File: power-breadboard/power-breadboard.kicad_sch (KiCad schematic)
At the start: 0 parts

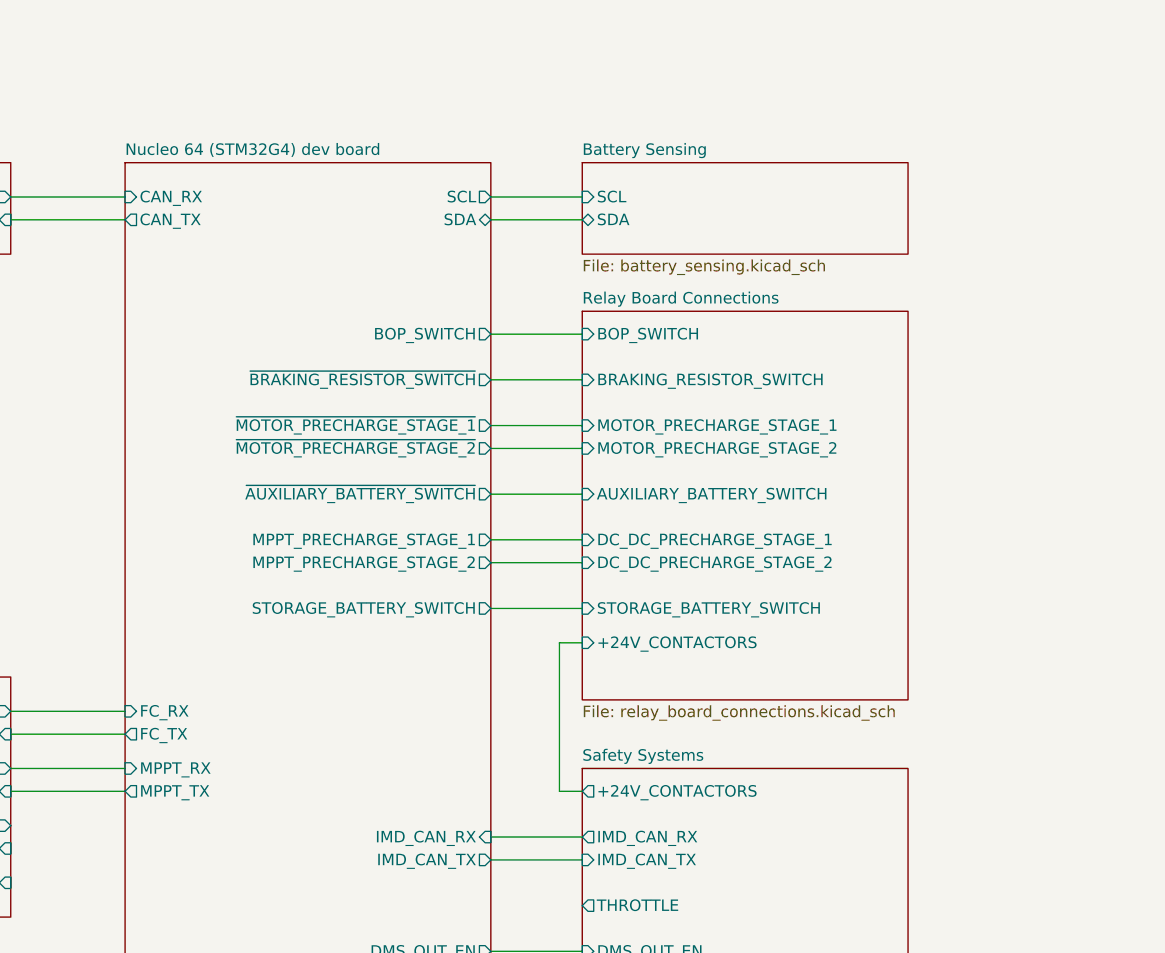
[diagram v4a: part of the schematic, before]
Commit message: power-breadboard: finish relay board connections
Updateed to use separarate relay boards. Also updated hierarchical
labels and sheet pins.
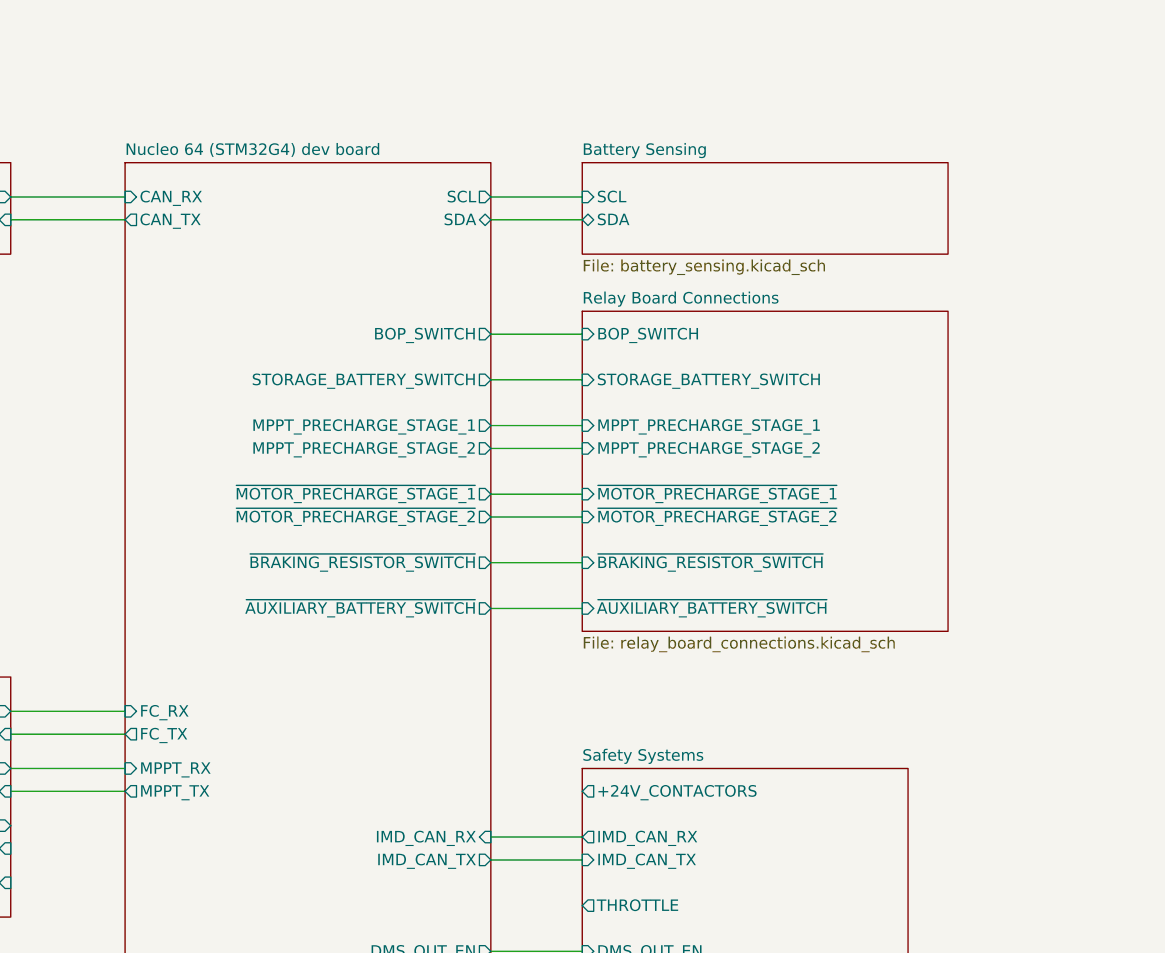
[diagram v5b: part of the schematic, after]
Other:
- sheet Relay Board Connections ports: added MPPT_PRECHARGE_STAGE_1, MPPT_PRECHARGE_STAGE_2, ~{AUXILIARY_BATTERY_SWITCH}, ~{BRAKING_RESISTOR_SWITCH}, ~{MOTOR_PRECHARGE_STAGE_1}, ~{MOTOR_PRECHARGE_STAGE_2}; removed +24V_CONTACTORS, AUXILIARY_BATTERY_SWITCH, BRAKING_RESISTOR_SWITCH, DC_DC_PRECHARGE_STAGE_1, DC_DC_PRECHARGE_STAGE_2, MOTOR_PRECHARGE_STAGE_1, MOTOR_PRECHARGE_STAGE_2
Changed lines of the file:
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@@
 	(wire
 		(pts
-			(xy 147.32 54.61) (xy 157.48 54.61)
+			(xy 147.32 74.93) (xy 157.48 74.93)
 		)
 		(stroke
@@
 	(wire
 		(pts
-			(xy 147.32 80.01) (xy 157.48 80.01)
+			(xy 147.32 54.61) (xy 157.48 54.61)
 		)
 		(stroke
@@
 	(wire
 		(pts
-			(xy 147.32 62.23) (xy 157.48 62.23)
-		)
-		(stroke
-			(width 0)
-			(type default)
-		)
-	)
-	(wire
-		(pts
-			(xy 154.94 100.33) (xy 154.94 83.82)
+			(xy 147.32 69.85) (xy 157.48 69.85)
 		)
 		(stroke
@@
 	(wire
 		(pts
-			(xy 147.32 59.69) (xy 157.48 59.69)
+			(xy 147.32 67.31) (xy 157.48 67.31)
 		)
 		(stroke
@@
 	(wire
 		(pts
-			(xy 147.32 67.31) (xy 157.48 67.31)
+			(xy 147.32 80.01) (xy 157.48 80.01)
 		)
 		(stroke
@@
 	(wire
 		(pts
-			(xy 147.32 74.93) (xy 157.48 74.93)
-		)
-		(stroke
-			(width 0)
-			(type default)
-		)
-	)
-	(wire
-		(pts
-			(xy 157.48 100.33) (xy 154.94 100.33)
+			(xy 147.32 62.23) (xy 157.48 62.23)
 		)
 		(stroke
@@
 	(wire
 		(pts
-			(xy 154.94 83.82) (xy 157.48 83.82)
-		)
-		(stroke
-			(width 0)
-			(type default)
-		)
-	)
-	(wire
-		(pts
-			(xy 147.32 72.39) (xy 157.48 72.39)
+			(xy 147.32 59.69) (xy 157.48 59.69)
 		)
 		(stroke
@@
 	(sheet
 		(at 157.48 30.48)
-		(size 36.195 10.16)
+		(size 40.64 10.16)
 		(exclude_from_sim no)
 		(in_bom yes)
@@
 		)
 		(pin "MPPT_PRECHARGE_STAGE_1" output
-			(at 147.32 72.39 0)
+			(at 147.32 59.69 0)
 			(effects
 				(font
@@
 		)
 		(pin "MPPT_PRECHARGE_STAGE_2" output
-			(at 147.32 74.93 0)
+			(at 147.32 62.23 0)
 			(effects
 				(font
@@
 		)
 		(pin "STORAGE_BATTERY_SWITCH" output
-			(at 147.32 80.01 0)
+			(at 147.32 54.61 0)
 			(effects
 				(font
@@
 		)
 		(pin "~{AUXILIARY_BATTERY_SWITCH}" output
+			(at 147.32 80.01 0)
+			(effects
+				(font
+					(size 1.27 1.27)
+				)
+				(justify right)
+			)
+		)
+		(pin "~{BRAKING_RESISTOR_SWITCH}" output
+			(at 147.32 74.93 0)
+			(effects
+				(font
+					(size 1.27 1.27)
+				)
+				(justify right)
+			)
+		)
+		(pin "~{MOTOR_PRECHARGE_STAGE_1}" output
 			(at 147.32 67.31 0)
 			(effects
@@
 			)
 		)
-		(pin "~{BRAKING_RESISTOR_SWITCH}" output
-			(at 147.32 54.61 0)
-			(effects
-				(font
-					(size 1.27 1.27)
-				)
-				(justify right)
-			)
-		)
-		(pin "~{MOTOR_PRECHARGE_STAGE_1}" output
-			(at 147.32 59.69 0)
-			(effects
-				(font
-					(size 1.27 1.27)
-				)
-				(justify right)
-			)
-		)
 		(pin "~{MOTOR_PRECHARGE_STAGE_2}" output
-			(at 147.32 62.23 0)
+			(at 147.32 69.85 0)
 			(effects
 				(font
@@
 	(sheet
 		(at 157.48 46.99)
-		(size 36.195 43.18)
+		(size 40.64 35.56)
 		(exclude_from_sim no)
 		(in_bom yes)
@@
 		)
 		(property "Sheetfile" "relay_board_connections.kicad_sch"
-			(at 157.48 90.7546 0)
+			(at 157.48 83.1346 0)
 			(show_name no)
 			(do_not_autoplace no)
@@
 		)
 		(pin "STORAGE_BATTERY_SWITCH" input
-			(at 157.48 80.01 180)
-			(effects
-				(font
-					(size 1.27 1.27)
-				)
-				(justify left)
-			)
-		)
-		(pin "DC_DC_PRECHARGE_STAGE_2" input
-			(at 157.48 74.93 180)
-			(effects
-				(font
-					(size 1.27 1.27)
-				)
-				(justify left)
-			)
-		)
-		(pin "DC_DC_PRECHARGE_STAGE_1" input
-			(at 157.48 72.39 180)
-			(effects
-				(font
-					(size 1.27 1.27)
-				)
-				(justify left)
-			)
-		)
-		(pin "AUXILIARY_BATTERY_SWITCH" input
-			(at 157.48 67.31 180)
-			(effects
-				(font
-					(size 1.27 1.27)
-				)
-				(justify left)
-			)
-		)
-		(pin "MOTOR_PRECHARGE_STAGE_2" input
-			(at 157.48 62.23 180)
-			(effects
-				(font
-					(size 1.27 1.27)
-				)
-				(justify left)
-			)
-		)
-		(pin "MOTOR_PRECHARGE_STAGE_1" input
-			(at 157.48 59.69 180)
-			(effects
-				(font
-					(size 1.27 1.27)
-				)
-				(justify left)
-			)
-		)
-		(pin "BRAKING_RESISTOR_SWITCH" input
 			(at 157.48 54.61 180)
 			(effects
@@
 			)
 		)
-		(pin "+24V_CONTACTORS" input
-			(at 157.48 83.82 180)
-			(effects
-				(font
+		(pin "MPPT_PRECHARGE_STAGE_1" input
+			(at 157.48 59.69 180)
+			(effects
+				(font
+					(size 1.27 1.27)
+				)
+				(justify left)
+			)
+		)
+		(pin "MPPT_PRECHARGE_STAGE_2" input
+			(at 157.48 62.23 180)
+			(effects
+				(font
+					(size 1.27 1.27)
+				)
+				(justify left)
+			)
+		)
+		(pin "~{AUXILIARY_BATTERY_SWITCH}" input
+			(at 157.48 80.01 180)
+			(effects
+				(font
+					(size 1.27 1.27)
+				)
+				(justify left)
+			)
+		)
+		(pin "~{BRAKING_RESISTOR_SWITCH}" input
+			(at 157.48 74.93 180)
+			(effects
+				(font
+					(size 1.27 1.27)
+				)
+				(justify left)
+			)
+		)
+		(pin "~{MOTOR_PRECHARGE_STAGE_1}" input
+			(at 157.48 67.31 180)
+			(effects
+				(font
+					(size 1.27 1.27)
+				)
+				(justify left)
+			)
+		)
+		(pin "~{MOTOR_PRECHARGE_STAGE_2}" input
+			(at 157.48 69.85 180)
+			(effects
+				(font

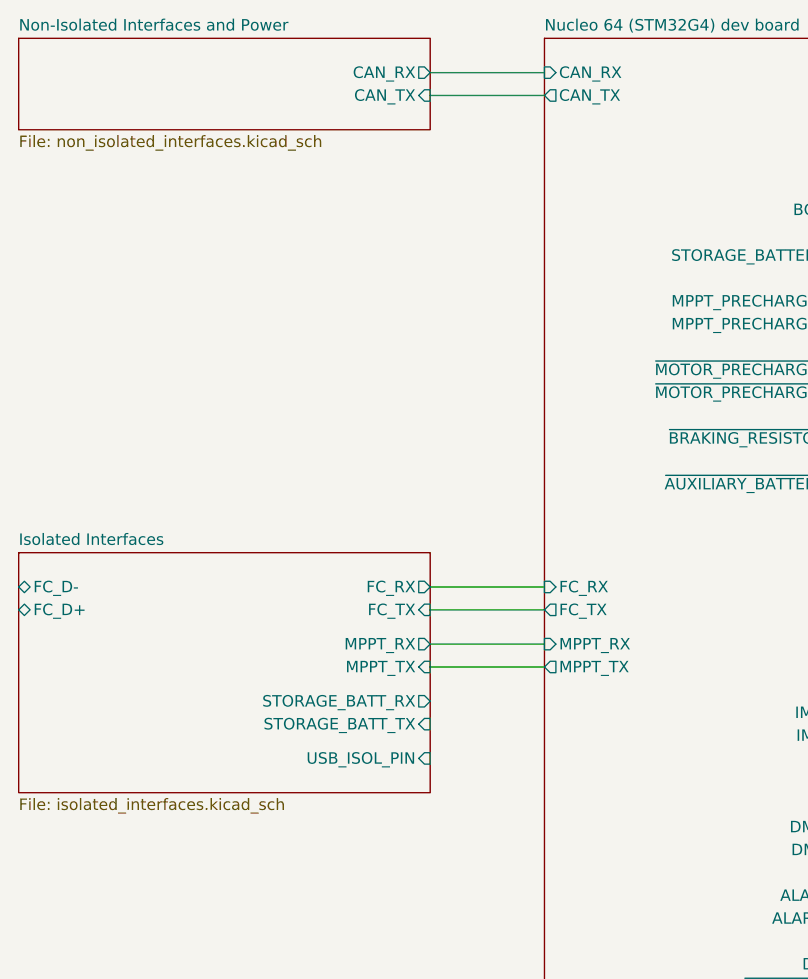
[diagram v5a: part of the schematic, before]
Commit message: power-breadboard: change DC+ of 4-relay board
Needs to be 24V instead of 5V.
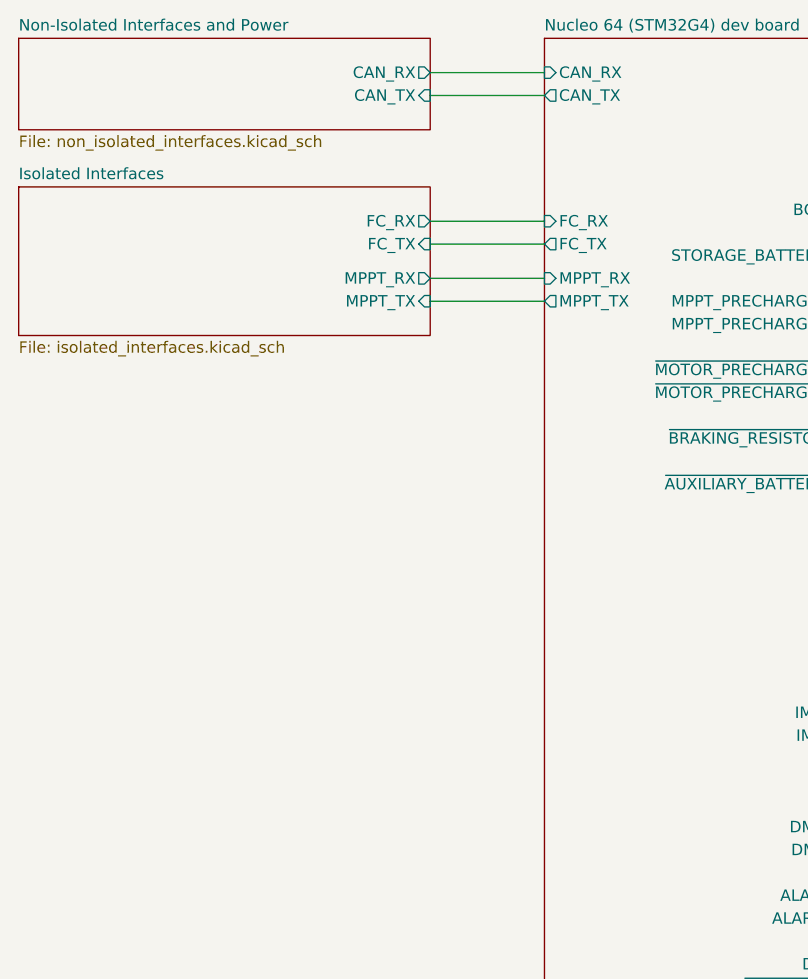
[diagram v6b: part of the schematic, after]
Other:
- sheet Isolated Interfaces ports: added none; removed FC_D+, FC_D-, STORAGE_BATT_RX, STORAGE_BATT_TX, USB_ISOL_PIN
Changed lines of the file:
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@@
 	(wire
 		(pts
-			(xy 93.98 91.44) (xy 106.68 91.44)
+			(xy 93.98 50.8) (xy 106.68 50.8)
 		)
 		(stroke
@@
 	(wire
 		(pts
-			(xy 93.98 97.79) (xy 106.68 97.79)
+			(xy 93.98 57.15) (xy 106.68 57.15)
 		)
 		(stroke
@@
 	(wire
 		(pts
-			(xy 93.98 93.98) (xy 106.68 93.98)
+			(xy 93.98 53.34) (xy 106.68 53.34)
 		)
 		(stroke
@@
 	(wire
 		(pts
-			(xy 93.98 100.33) (xy 106.68 100.33)
+			(xy 93.98 59.69) (xy 106.68 59.69)
 		)
 		(stroke
@@
 		)
 		(pin "FC_RX" input
-			(at 106.68 91.44 180)
+			(at 106.68 50.8 180)
 			(effects
 				(font
@@
 		)
 		(pin "FC_TX" output
-			(at 106.68 93.98 180)
+			(at 106.68 53.34 180)
 			(effects
 				(font
@@
 		)
 		(pin "MPPT_RX" input
-			(at 106.68 97.79 180)
+			(at 106.68 57.15 180)
 			(effects
 				(font
@@
 		)
 		(pin "MPPT_TX" output
-			(at 106.68 100.33 180)
+			(at 106.68 59.69 180)
 			(effects
 				(font
@@
 	)
 	(sheet
-		(at 48.26 87.63)
-		(size 45.72 26.67)
+		(at 48.26 46.99)
+		(size 45.72 16.51)
 		(exclude_from_sim no)
 		(in_bom yes)
@@
 		)
 		(property "Sheetname" "Isolated Interfaces"
-			(at 48.26 86.9184 0)
+			(at 48.26 46.2784 0)
 			(show_name no)
 			(do_not_autoplace no)
@@
 		)
 		(property "Sheetfile" "isolated_interfaces.kicad_sch"
-			(at 48.26 114.8846 0)
+			(at 48.26 64.0846 0)
 			(show_name no)
 			(do_not_autoplace no)
@@
 			)
 		)
-		(pin "FC_D+" bidirectional
-			(at 48.26 93.98 180)
-			(effects
-				(font
-					(size 1.27 1.27)
-				)
-				(justify left)
-			)
-		)
-		(pin "FC_D-" bidirectional
-			(at 48.26 91.44 180)
-			(effects
-				(font
-					(size 1.27 1.27)
-				)
-				(justify left)
-			)
-		)
 		(pin "FC_RX" output
-			(at 93.98 91.44 0)
+			(at 93.98 50.8 0)
 			(effects
 				(font
@@
 		)
 		(pin "FC_TX" input
-			(at 93.98 93.98 0)
+			(at 93.98 53.34 0)
 			(effects
 				(font
@@
 		)
 		(pin "MPPT_RX" output
-			(at 93.98 97.79 0)
+			(at 93.98 57.15 0)
 			(effects
 				(font
@@
 		)
 		(pin "MPPT_TX" input
-			(at 93.98 100.33 0)
-			(effects
-				(font
-					(size 1.27 1.27)
-				)
-				(justify right)
-			)
-		)
-		(pin "USB_ISOL_PIN" input
-			(at 93.98 110.49 0)
-			(effects
-				(font
-					(size 1.27 1.27)
-				)
-				(justify right)
-			)
-		)
-		(pin "STORAGE_BATT_TX" input
-			(at 93.98 106.68 0)
-			(effects
-				(font
-					(size 1.27 1.27)
-				)
-				(justify right)
-			)
-		)
-		(pin "STORAGE_BATT_RX" output
-			(at 93.98 104.14 0)
-			(effects
-				(font
+			(at 93.98 59.69 0)
+			(effects
+				(font
